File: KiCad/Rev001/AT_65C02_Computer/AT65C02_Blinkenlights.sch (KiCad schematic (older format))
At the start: 20 parts, among them U20 74HCT540, U21 74HCT573, U22 74HCT573, U23 74HCT573, U24 10_LED_Array, U25 10_LED_Array, U26 10_LED_Array, U27 10_LED_Array

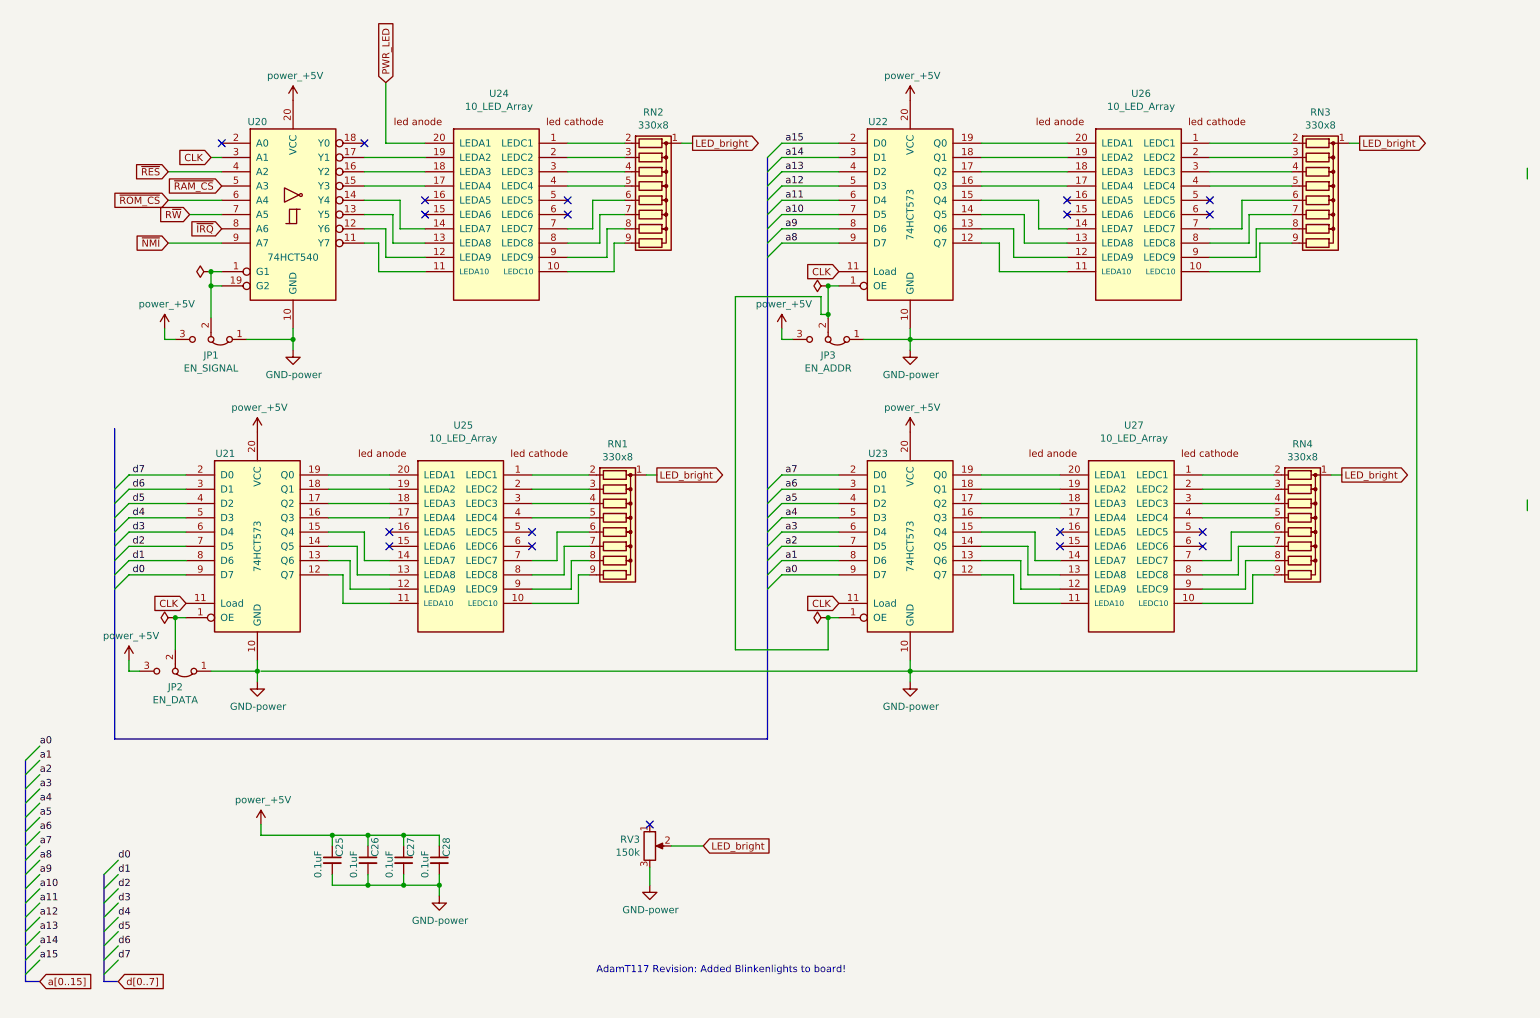
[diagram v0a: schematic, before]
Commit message: HEX Board Mods
Hex board changes. Main board Hex to Latches
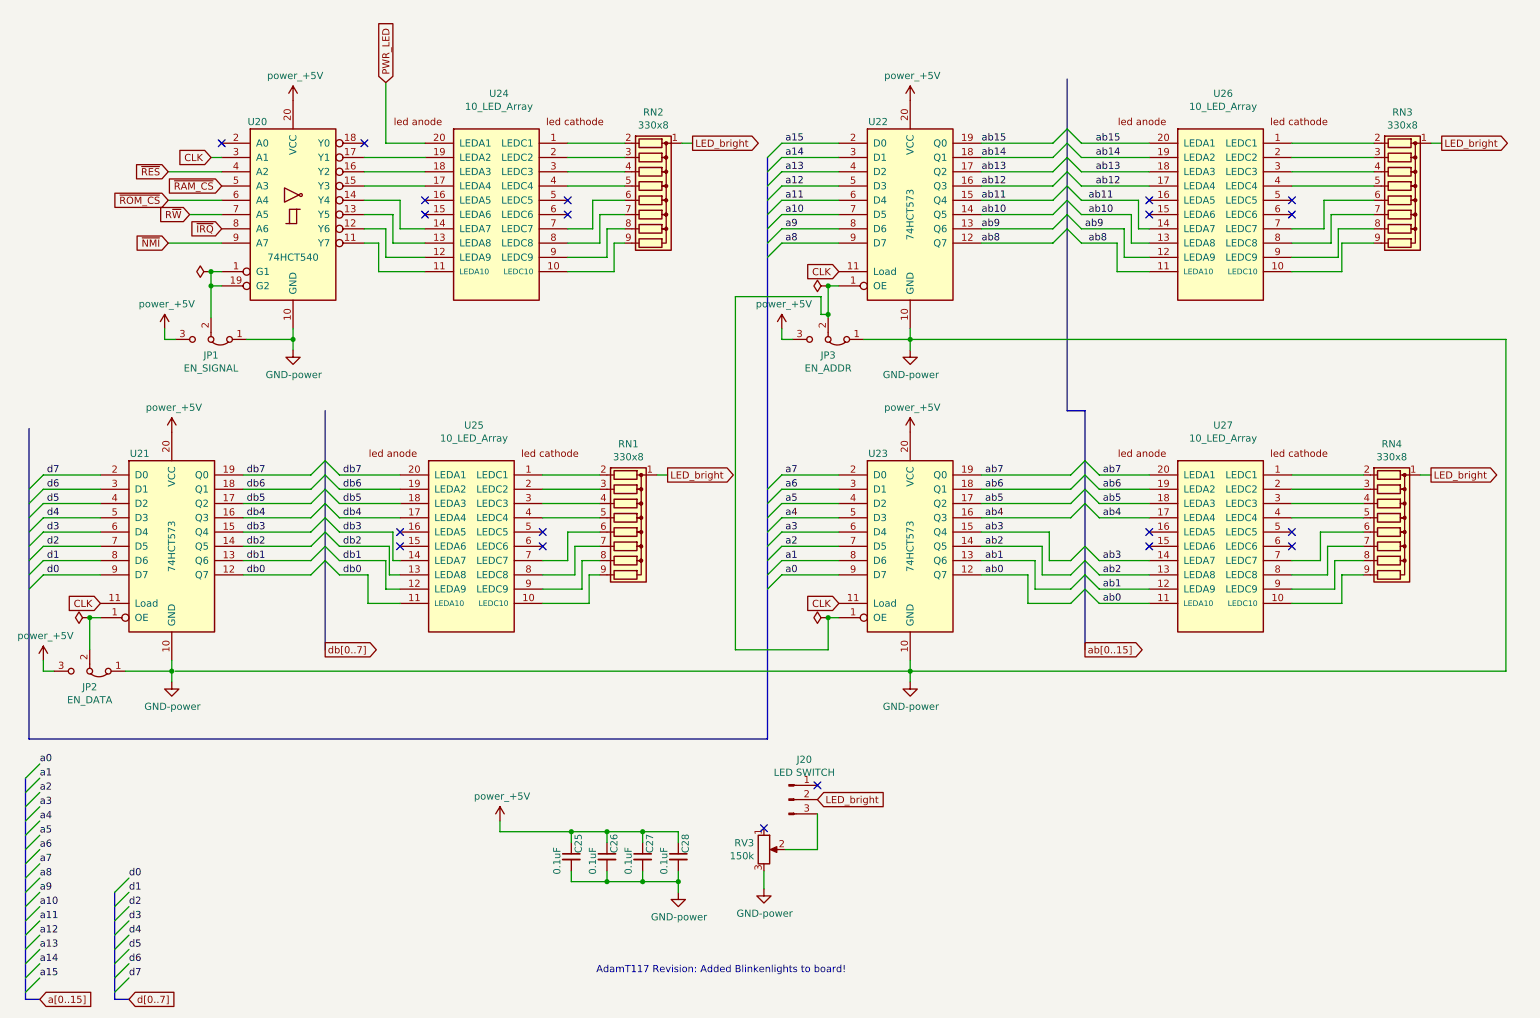
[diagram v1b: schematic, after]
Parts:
- added J20: LED SWITCH, Connector_PinHeader_2.54mm:PinHeader_1x03_P2.54mm_Vertical, symbol 65C02_Computer-rescue:Conn_01x03_Male-Connector
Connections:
- net LED_bright: now also J20.2 (Pin_2); no longer RV3.2
- net db0: now reaches U21.12 (Q7), U25.11 (LEDA10)
- net db1: now reaches U21.13 (Q6), U25.12 (LEDA9)
- net db2: now reaches U21.14 (Q5), U25.13 (LEDA8)
- net db3: now reaches U21.15 (Q4), U25.14 (LEDA7)
- net db4: now reaches U21.16 (Q3), U25.17 (LEDA4)
- net db5: now reaches U21.17 (Q2), U25.18 (LEDA3)
- net db6: now reaches U21.18 (Q1), U25.19 (LEDA2)
- net db7: now reaches U21.19 (Q0), U25.20 (LEDA1)
- net ab0: now reaches U23.12 (Q7), U27.11 (LEDA10)
- net ab1: now reaches U23.13 (Q6), U27.12 (LEDA9)
- net ab2: now reaches U23.14 (Q5), U27.13 (LEDA8)
- net ab3: now reaches U23.15 (Q4), U27.14 (LEDA7)
- net ab4: now reaches U23.16 (Q3), U27.17 (LEDA4)
- net ab5: now reaches U23.17 (Q2), U27.18 (LEDA3)
- net ab6: now reaches U23.18 (Q1), U27.19 (LEDA2)
- net ab7: now reaches U23.19 (Q0), U27.20 (LEDA1)
- net ab8: now reaches U22.12 (Q7), U26.11 (LEDA10)
- net ab9: now reaches U22.13 (Q6), U26.12 (LEDA9)
- net ab10: now reaches U22.14 (Q5), U26.13 (LEDA8)
- net ab11: now reaches U22.15 (Q4), U26.14 (LEDA7)
- net ab12: now reaches U22.16 (Q3), U26.17 (LEDA4)
- net ab13: now reaches U22.17 (Q2), U26.18 (LEDA3)
- net ab14: now reaches U22.18 (Q1), U26.19 (LEDA2)
- net ab15: now reaches U22.19 (Q0), U26.20 (LEDA1)
- new net: J20.3 (Pin_3), RV3.2
- no-connect marks 19 -> 20
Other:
- moved on the sheet: C25, C26, C27, C28, JP2, RN1, RN3, RN4, RV3, U21, U25, U26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
